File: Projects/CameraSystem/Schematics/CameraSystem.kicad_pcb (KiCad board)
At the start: 2 copper layers, 100 x 100 mm, 119 parts, among them J1 10118192-0001LF, J10 Conn_02x02_Odd_Even, J11 Conn_01x06, J12 Conn_01x06, J13 Conn_02x02_Odd_Even, J14 Conn_02x05_Odd_Even, J2 Conn_02x03_Odd_Even, J3 Conn_01x02, J4 Conn_01x03, J5 Conn_01x02, J6 Conn_02x02_Odd_Even, J7 Conn_02x02_Odd_Even, J8 DM3D-SF, J9 Conn_02x02_Odd_Even, K1 TouchPad, K2 TouchPad, K3 TouchPad, K4 TouchPad, K5 TouchPad, K6 TouchPad, K7 TouchPad, Q1 BC846B_215, Q2 BC846B_215, Q3 BC846B_215, Q4 BC846B_215, U1 CH340, U10 AT42QT1070-SSUR, U2 AZ1117CD-3.3TRG1DICT-ND, U3 ATMEGA16A-AU, U4 ESP8266, U5 MC74HC125ADTR2G, U6 OV7670, U7 SIT2001BI-S2-33E-24.000000G, U8 PCA9306D_118, U9 LCD_2x16_w_i2c, Y1 ABLS-12.000MHZ-B2-T, Y2 ABLS2-10.000MHZ-D4Y-T

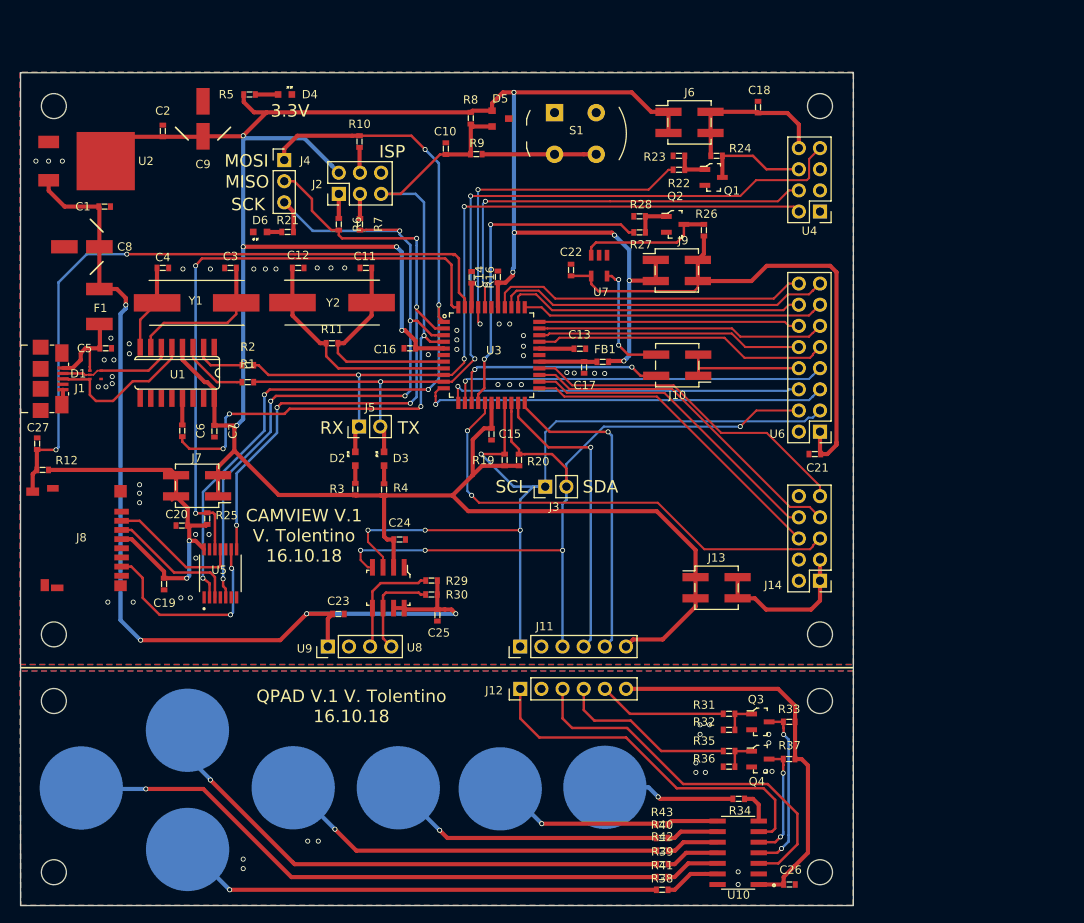
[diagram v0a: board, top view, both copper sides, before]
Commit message: camera was updated
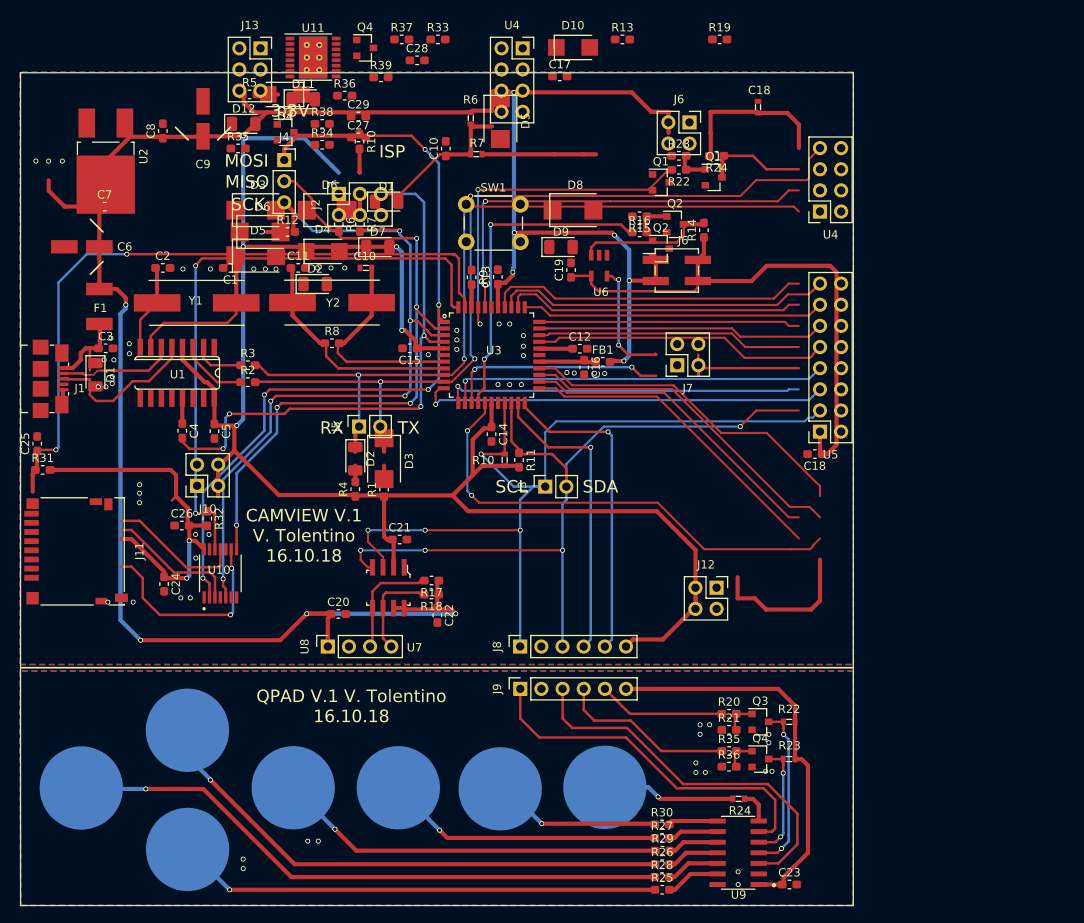
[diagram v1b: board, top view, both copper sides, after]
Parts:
- removed the C6 at (39.4, 63.0)
- removed the D1 at (29.0, 56.3)
- removed the D2 at (60.2, 66.3)
- removed the D3 at (63.7, 66.3)
- removed the D4 at (51.8, 22.6)
- removed the D5 at (77.6, 25.5)
- removed the D6 at (48.8, 39.1)
- removed J14: Conn_02x05_Odd_Even, Pin_Headers:Pin_Header_Straight_2x05_Pitch2.54mm
- removed the Q1 at (103.2, 32.6)
- removed the Q2 at (98.6, 38.2)
- removed the Q3 at (108.8, 97.9)
- removed the Q4 at (108.8, 102.4)
- removed the R35 at (105.1, 101.4)
- removed the R36 at (105.1, 103.3)
- removed R40, R41, R42, R43: 4K7, digikey-footprints:0603
- removed REF** (x8): MountingHole_3mm, Mounting_Holes:MountingHole_3mm
- removed S1: KS-01Q-01, digikey-footprints:PushButton_Round_D12mm_THT_KS-01Q-01
- removed the U4 at (116.0, 36.7)
- removed the U6 at (116.0, 63.1)
- removed the U9 at (56.9, 88.9)
- added C11: 27p, Capacitor_SMD:C_0603_1608Metric_Pad1.05x0.95mm_HandSolder, F.Cu at (53.3, 43.4)
- added C18: 100n, Capacitor_SMD:C_0603_1608Metric_Pad1.05x0.95mm_HandSolder, F.Cu at (115.4, 65.8)
- added C28: 2u2, Capacitor_SMD:C_0603_1608Metric_Pad1.05x0.95mm_HandSolder, F.Cu at (67.6, 18.5)
- added C29: 10u, Capacitor_SMD:C_0603_1608Metric_Pad1.05x0.95mm_HandSolder, F.Cu at (60.6, 25.3)
- added C8: 1u, Capacitor_SMD:C_0603_1608Metric_Pad1.05x0.95mm_HandSolder, F.Cu at (37.1, 27.0)
- added D1: BLUE_LED, LED_SMD:LED_1206_3216Metric, F.Cu at (64.0, 35.5)
- added D1: BLUE_LED, LED_SMD:LED_1206_3216Metric, F.Cu at (29.0, 56.3)
- added D10: SS14, custom-footprints:SMA_DO-214AC, F.Cu at (86.3, 17.0)
- added D11: GREEN_LED, LED_SMD:LED_1206_3216Metric, F.Cu at (53.9, 23.2)
- added D12: RED_LED, LED_SMD:LED_1206_3216Metric, F.Cu at (46.8, 26.1)
- added D2: YELLOW_LED, LED_SMD:LED_1206_3216Metric, F.Cu at (55.4, 45.4)
- added D2: YELLOW_LED, LED_SMD:LED_1206_3216Metric, F.Cu at (60.2, 66.3)
- added D3: SMBJ5.0CA, custom-footprints:SMB_DO-214AA, F.Cu at (48.2, 36.5)
- added D3: SMBJ5.0CA, custom-footprints:SMB_DO-214AA, F.Cu at (63.7, 66.3)
- added D4: SS14, custom-footprints:SMA_DO-214AC, F.Cu at (56.3, 41.5)
- added D4: SS14, custom-footprints:SMA_DO-214AC, F.Cu at (51.8, 22.6)
- added D5: SMBJ5.0CA, custom-footprints:SMB_DO-214AA, F.Cu at (48.2, 42.0)
- added D5: SMBJ5.0CA, custom-footprints:SMB_DO-214AA, F.Cu at (77.6, 25.5)
- added D6: SMBJ5.0CA, custom-footprints:SMB_DO-214AA, F.Cu at (56.8, 36.5)
- added D6: SMBJ5.0CA, custom-footprints:SMB_DO-214AA, F.Cu at (48.8, 39.1)
- added D7: GREEN_LED, LED_SMD:LED_1206_3216Metric, F.Cu at (62.9, 40.9)
- added D8: SMBJ5.0CA, custom-footprints:SMB_DO-214AA, F.Cu at (86.3, 36.5)
- added D9: LED, LED_SMD:LED_1206_3216Metric, F.Cu at (84.9, 40.9)
- added J9: Conn_01x06, Connector_PinSocket_2.54mm:PinSocket_1x06_P2.54mm_Vertical, F.Cu at (80.0, 94.0)
- added Q1: BC847, Package_TO_SOT_SMD:SOT-23, F.Cu at (96.9, 33.2)
- added Q1: BC847, Package_TO_SOT_SMD:SOT-23, F.Cu at (103.2, 32.6)
- added Q2: BC847, Package_TO_SOT_SMD:SOT-23, F.Cu at (96.9, 41.1)
- added Q2: BC847, Package_TO_SOT_SMD:SOT-23, F.Cu at (98.6, 38.2)
- added Q3: BC847, Package_TO_SOT_SMD:SOT-23, F.Cu at (51.8, 27.2)
- added Q3: BC847, Package_TO_SOT_SMD:SOT-23, F.Cu at (108.8, 97.9)
- added Q4: BC847, Package_TO_SOT_SMD:SOT-23, F.Cu at (61.4, 17.0)
- added Q4: BC847, Package_TO_SOT_SMD:SOT-23, F.Cu at (108.8, 102.4)
- added R13: 10k, Resistor_SMD:R_0603_1608Metric_Pad1.05x0.95mm_HandSolder, F.Cu at (92.3, 16.0)
- added R14: 10k, Resistor_SMD:R_0603_1608Metric_Pad1.05x0.95mm_HandSolder, F.Cu at (102.1, 38.9)
- added R15: 10k, Resistor_SMD:R_0603_1608Metric_Pad1.05x0.95mm_HandSolder, F.Cu at (94.3, 37.2)
- added R17: 1K74, Resistor_SMD:R_0603_1608Metric_Pad1.05x0.95mm_HandSolder, F.Cu at (69.4, 81.0)
- added R18: 1K74, Resistor_SMD:R_0603_1608Metric_Pad1.05x0.95mm_HandSolder, F.Cu at (69.3, 82.7)
- added R19: 200k, Resistor_SMD:R_0603_1608Metric_Pad1.05x0.95mm_HandSolder, F.Cu at (104.0, 16.0)
- added R33: 1, Resistor_SMD:R_0603_1608Metric_Pad1.05x0.95mm_HandSolder, F.Cu at (70.1, 16.0)
- added R34: 10k, Resistor_SMD:R_0603_1608Metric_Pad1.05x0.95mm_HandSolder, F.Cu at (56.2, 28.6)
- added R35: 10k, Resistor_SMD:R_0603_1608Metric_Pad1.05x0.95mm_HandSolder, F.Cu at (46.1, 29.1)
- added R35: 10k, Resistor_SMD:R_0603_1608Metric_Pad1.05x0.95mm_HandSolder, F.Cu at (105.1, 101.4)
- added R36: 47k, Resistor_SMD:R_0603_1608Metric_Pad1.05x0.95mm_HandSolder, F.Cu at (58.9, 22.7)
- added R36: 47k, Resistor_SMD:R_0603_1608Metric_Pad1.05x0.95mm_HandSolder, F.Cu at (105.1, 103.3)
- added R37: 560, Resistor_SMD:R_0603_1608Metric_Pad1.05x0.95mm_HandSolder, F.Cu at (65.8, 16.0)
- added R8: 1M, Resistor_SMD:R_0603_1608Metric_Pad1.05x0.95mm_HandSolder, F.Cu at (57.4, 52.5)
- added R9: 10k, Resistor_SMD:R_0603_1608Metric_Pad1.05x0.95mm_HandSolder, F.Cu at (74.2, 44.6)
- added SW1: SW_Push, Button_Switch_THT:SW_PUSH_6mm_H4.3mm, F.Cu at (73.5, 35.8)
- added U11: DRV8833PWP, Package_SO:HTSSOP-16-1EP_4.4x5mm_P0.65mm_EP3.4x5mm_Mask2.46x2.31mm_ThermalVias, F.Cu at (55.1, 18.2)
- added U4: ESP8266, Connector_PinSocket_2.54mm:PinSocket_2x04_P2.54mm_Vertical, F.Cu at (80.3, 17.1)
- added U4: ESP8266, Connector_PinSocket_2.54mm:PinSocket_2x04_P2.54mm_Vertical, F.Cu at (116.0, 36.7)
- added U5: OV7670, Connector_PinSocket_2.54mm:PinSocket_2x08_P2.54mm_Vertical, F.Cu at (116.0, 63.1)
- added U8: LCD_2x16_w_i2c, Connector_PinSocket_2.54mm:PinSocket_1x04_P2.54mm_Vertical, F.Cu at (56.9, 88.9)
- C1, C2: value 1u -> 27p; footprint digikey-footprints:0603 -> Capacitor_SMD:C_0603_1608Metric_Pad1.05x0.95mm_HandSolder
- C10: value 100n -> 27p; footprint digikey-footprints:0603 -> Capacitor_SMD:C_0603_1608Metric_Pad1.05x0.95mm_HandSolder
- C12, C3: value 27p -> 100n; footprint digikey-footprints:0603 -> Capacitor_SMD:C_0603_1608Metric_Pad1.05x0.95mm_HandSolder
- C13, C14, C15, C16, C17, C19, C20, C21, C22, C23, C24, C25, C26, C5: footprint digikey-footprints:0603 -> Capacitor_SMD:C_0603_1608Metric_Pad1.05x0.95mm_HandSolder
- C27: value 100n -> 10n; footprint digikey-footprints:0603 -> Capacitor_SMD:C_0603_1608Metric_Pad1.05x0.95mm_HandSolder
- C4: value 22p -> 100n; footprint digikey-footprints:0603 -> Capacitor_SMD:C_0603_1608Metric_Pad1.05x0.95mm_HandSolder
- C7: value 100n -> 1u; footprint digikey-footprints:0603 -> Capacitor_SMD:C_0603_1608Metric_Pad1.05x0.95mm_HandSolder
- FB1, R2, R4, R5, R7: footprint digikey-footprints:0603 -> Resistor_SMD:R_0603_1608Metric_Pad1.05x0.95mm_HandSolder
- J10, J6, J7: footprint Pin_Headers:Pin_Header_Straight_2x02_Pitch2.54mm_SMD -> Connector_PinSocket_2.54mm:PinSocket_2x02_P2.54mm_Vertical
- J11: value Conn_01x06 -> DM3D-SF; footprint Pin_Headers:Pin_Header_Straight_1x06_Pitch2.54mm -> Connector_Card:microSD_HC_Hirose_DM3D-SF
- J12: value Conn_01x06 -> Conn_02x02_Odd_Even; footprint Pin_Headers:Pin_Header_Straight_1x06_Pitch2.54mm -> Connector_PinSocket_2.54mm:PinSocket_2x02_P2.54mm_Vertical
- J13: value Conn_02x02_Odd_Even -> Conn_02x03_Odd_Even; footprint Pin_Headers:Pin_Header_Straight_2x02_Pitch2.54mm_SMD -> Connector_PinSocket_2.54mm:PinSocket_2x03_P2.54mm_Vertical
- J2: footprint Pin_Headers:Pin_Header_Straight_2x03_Pitch2.54mm -> Connector_PinSocket_2.54mm:PinSocket_2x03_P2.54mm_Vertical
- J3, J5: footprint Pin_Headers:Pin_Header_Straight_1x02_Pitch2.54mm -> Connector_PinSocket_2.54mm:PinSocket_1x02_P2.54mm_Vertical
- J4: footprint Pin_Headers:Pin_Header_Straight_1x03_Pitch2.54mm -> Connector_PinSocket_2.54mm:PinSocket_1x03_P2.54mm_Vertical
- J8: value DM3D-SF -> Conn_01x06; footprint custom-footprints:DM3D-SF -> Connector_PinSocket_2.54mm:PinSocket_1x06_P2.54mm_Vertical
- R1: value 1k -> 560; footprint digikey-footprints:0603 -> Resistor_SMD:R_0603_1608Metric_Pad1.05x0.95mm_HandSolder
- R10: value 330 -> 2K2; footprint digikey-footprints:0603 -> Resistor_SMD:R_0603_1608Metric_Pad1.05x0.95mm_HandSolder
- R11: value 1M -> 2K2; footprint digikey-footprints:0603 -> Resistor_SMD:R_0603_1608Metric_Pad1.05x0.95mm_HandSolder
- R12: value 10k -> 560; footprint digikey-footprints:0603 -> Resistor_SMD:R_0603_1608Metric_Pad1.05x0.95mm_HandSolder
- R16: value 10k -> 4k7; footprint digikey-footprints:0603 -> Resistor_SMD:R_0603_1608Metric_Pad1.05x0.95mm_HandSolder
- R20: value 2K2 -> 4K7; footprint digikey-footprints:0603 -> Resistor_SMD:R_0603_1608Metric_Pad1.05x0.95mm_HandSolder
- R21: value 560 -> 10K; footprint digikey-footprints:0603 -> Resistor_SMD:R_0603_1608Metric_Pad1.05x0.95mm_HandSolder
- R22: value 4K7 -> 10K; footprint digikey-footprints:0603 -> Resistor_SMD:R_0603_1608Metric_Pad1.05x0.95mm_HandSolder
- R23: value 10k -> 10K; footprint digikey-footprints:0603 -> Resistor_SMD:R_0603_1608Metric_Pad1.05x0.95mm_HandSolder
- R24, R25, R26, R27: value 10k -> 4K7; footprint digikey-footprints:0603 -> Resistor_SMD:R_0603_1608Metric_Pad1.05x0.95mm_HandSolder
- R28: value 4k7 -> 4K7; footprint digikey-footprints:0603 -> Resistor_SMD:R_0603_1608Metric_Pad1.05x0.95mm_HandSolder
- R29, R30: value 1K74 -> 4K7; footprint digikey-footprints:0603 -> Resistor_SMD:R_0603_1608Metric_Pad1.05x0.95mm_HandSolder
- R3: value 560 -> 1k; footprint digikey-footprints:0603 -> Resistor_SMD:R_0603_1608Metric_Pad1.05x0.95mm_HandSolder
- R31: value 4K7 -> 10k; footprint digikey-footprints:0603 -> Resistor_SMD:R_0603_1608Metric_Pad1.05x0.95mm_HandSolder
- R32: value 10K -> 10k; footprint digikey-footprints:0603 -> Resistor_SMD:R_0603_1608Metric_Pad1.05x0.95mm_HandSolder
- R38: value 4K7 -> 47k; footprint digikey-footprints:0603 -> Resistor_SMD:R_0603_1608Metric_Pad1.05x0.95mm_HandSolder
- R39: value 4K7 -> 560; footprint digikey-footprints:0603 -> Resistor_SMD:R_0603_1608Metric_Pad1.05x0.95mm_HandSolder
- R6: value 330 -> 10k; footprint digikey-footprints:0603 -> Resistor_SMD:R_0603_1608Metric_Pad1.05x0.95mm_HandSolder
- U2: footprint custom-footprints:TO252-2 -> Package_TO_SOT_SMD:TO-252-2_TabPin1
- moved R38 100.6 mm to (56.2, 26.1)
- moved R39 100.3 mm to (63.3, 20.5)
- moved R31 87.5 mm to (22.7, 67.7)
- moved J13 84.8 mm to (48.8, 17.1)
- moved C26 84.7 mm to (39.4, 74.4)
- moved R21 79.9 mm to (105.1, 98.9)
- moved R28 77.5 mm to (97.0, 116.6)
- moved R26 76.3 mm to (97.1, 115.0), turned to 0 degrees
- moved R27 74.7 mm to (97.0, 111.9), turned to 0 degrees
- moved R25 70.5 mm to (97.1, 118.1), turned to 0 degrees
- moved R32 67.6 mm to (42.4, 73.5), turned to 270 degrees
- moved C23 63.2 mm to (112.3, 117.5)
- moved C19 61.7 mm to (86.1, 43.7), turned to 90 degrees
- moved J10 59.4 mm to (41.2, 69.6)
- moved J7 59.4 mm to (98.9, 55.1)
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- renumbered C11 to C10, C8 to C6, J9 to J6, R19 to R10, R33 to R22, R37 to R23, R34 to R24, R8 to R6, R9 to R7, U5 to U10, U7 to U6, U8 to U7, U10 to U9
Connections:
- C1 pad 1: /Display/VDD_5V0 -> Net-(C1-Pad1)
- C10 pad 1: Net-(C11-Pad1) -> Net-(C10-Pad1)
- C10 pad 1: /Input_Interface/SPI_RST -> Net-(C10-Pad1)
- C13 pad 1: Net-(C13-Pad1) -> /Camera/VDD_3V3
- C16 pad 1: /Camera/VDD_3V3 -> Net-(C16-Pad1)
- C17 pad 1: Net-(C17-Pad1) -> /Camera/VDD_3V3
- C18 pad 1: /Wifi/VDD_3V3_IN -> /Camera/VDD_3V3_IN
- C19 pad 1: /Memory/VDD_3V3_IN -> /Camera/VDD_3V3_IN
- C2 pad 1: /Camera/VDD_3V3 -> Net-(C2-Pad1)
- C20 pad 1: GND -> /Display/VDD_5V0
- C20 pad 2: /Memory/VDD_3V3_IN -> GND
- C21 pad 1: /Camera/VDD_3V3_IN -> /Camera/VDD_3V3
- C22 pad 1: /Camera/VDD_3V3_IN -> Net-(C22-Pad1)
- C23 pad 1: /Display/VDD_5V0 -> /Keypad/VDD_3V3
- C23 pad 2: GND -> /Keypad/QP_GND
- C24 pad 1: /Camera/VDD_3V3 -> /Memory/VDD_3V3_IN
- C25 pad 1: /Display/VDD_5V0 -> /Memory/_SD_DET
- C26 pad 1: /Keypad/VDD_3V3 -> GND
- C26 pad 2: /Keypad/QP_GND -> /Memory/VDD_3V3_IN
- C27 pad 1: /Memory/_SD_DET -> Net-(C27-Pad1)
- C27 pad 2: GND -> /Motor/VDD_3V3_CON_IN
- C4 pad 2: GND -> /Microcontroller/U2_SPI_RST
- C5 pad 1: Net-(C5-Pad1) -> /Camera/VDD_3V3
- C7 pad 1: /Camera/VDD_3V3 -> /Display/VDD_5V0
- F1 pad 2: Net-(C5-Pad1) -> Net-(C3-Pad1)
- FB1 pad 1: Net-(C17-Pad1) -> Net-(C16-Pad1)
- J1 pad 1: Net-(C5-Pad1) -> Net-(C3-Pad1)
- J1 pad 4: (no net) -> Net-(J1-Pad4)
- J10 pad 1: Net-(J10-Pad1) -> /Camera/VDD_3V3
- J10 pad 2: /Camera/CAM_CLK -> /Memory/VDD_3V3_IN
- J10 pad 3: Net-(J10-Pad1) -> /Camera/VDD_3V3
- J10 pad 4: Net-(J10-Pad4) -> /Memory/VDD_3V3_IN
- J11 pad 1: /Camera/SCL_3V3 -> Net-(J11-Pad1)
- J11 pad 2: GND -> /Memory/SD_CS_IN
- J11 pad 3: /Camera/SDA_3V3 -> /Memory/SD_DATA_IN
- J11 pad 4: /Microcontroller/QT_CHN -> /Memory/VDD_3V3_IN
- J11 pad 5: /Microcontroller/QT_RST -> /Memory/SD_CLK_IN
- J11 pad 6: /Camera/VDD_3V3 -> GND
- J12 pad 1: /Keypad/SCL_3V3 -> /Camera/VDD_3V3
- J12 pad 2: /Keypad/QP_GND -> /Motor/VDD_3V3_CON_IN
- J12 pad 3: /Keypad/SDA_3V3 -> /Camera/VDD_3V3
- J12 pad 4: /Keypad/QT_CHN -> /Motor/VDD_3V3_CON_IN
- J13 pad 1: /Camera/VDD_3V3 -> /Motor/M_PWM_OUT_1
- J13 pad 2: /Motor/VDD_3V3_CON_IN -> /Motor/M_PWM_OUT_1
- J13 pad 3: /Camera/VDD_3V3 -> /Motor/M_PWM_OUT_2
- J13 pad 4: /Motor/VDD_3V3_CON_IN -> /Motor/M_PWM_OUT_2
- J2 pad 1: Net-(J2-Pad1) -> /Microcontroller/MISO
- J2 pad 3: Net-(J2-Pad3) -> /Microcontroller/SCK
- J2 pad 4: Net-(J2-Pad4) -> /Microcontroller/MOSI
- J2 pad 5: /Input_Interface/SPI_RST -> /Microcontroller/U2_SPI_RST
- J6 pad 2: /Wifi/VDD_3V3_IN -> /Camera/VDD_3V3_IN
- J6 pad 4: /Wifi/VDD_3V3_IN -> /Camera/VDD_3V3_IN
- J7 pad 1: /Camera/VDD_3V3 -> Net-(J7-Pad1)
- J7 pad 2: /Memory/VDD_3V3_IN -> /Camera/CAM_CLK
- J7 pad 3: /Camera/VDD_3V3 -> Net-(J7-Pad1)
- J7 pad 4: /Memory/VDD_3V3_IN -> Net-(J7-Pad4)
- J8 pad 1: (no net) -> /Camera/SCL_3V3
- J8 pad 2: /Memory/SD_CS_IN -> GND
- J8 pad 3: /Memory/SD_DATA_IN -> /Camera/SDA_3V3
- J8 pad 4: /Memory/VDD_3V3_IN -> /Microcontroller/QT_CHN
- J8 pad 5: (no net) -> /Microcontroller/QT_RST
- J8 pad 6: GND -> /Camera/VDD_3V3
- R1 pad 1: Net-(R1-Pad1) -> /Camera/VDD_3V3
- R1 pad 2: /Microcontroller/SPI_TX -> Net-(D1-Pad2)
- R10 pad 1: /Microcontroller/MOSI -> /Camera/SCL_3V3
- R10 pad 2: Net-(J2-Pad4) -> /Camera/VDD_3V3
- R11 pad 1: Net-(C12-Pad1) -> /Camera/SDA_3V3
- R11 pad 2: Net-(C11-Pad1) -> /Camera/VDD_3V3
- R12 pad 1: /Memory/_SD_DET -> Net-(D9-Pad2)
- R12 pad 2: /Memory/VDD_3V3_IN -> /Microcontroller/SCK
- R16 pad 1: GND -> /Camera/CAM_XCLK_CTL
- R16 pad 2: Net-(R16-Pad2) -> Net-(Q1-Pad1)
- R2 pad 2: /Microcontroller/SPI_RX -> /Microcontroller/UC_SPI_TX
- R20 pad 1: /Camera/SDA_3V3 -> /Keypad/QT_RST
- R20 pad 2: /Camera/VDD_3V3 -> Net-(Q2-Pad1)
- R21 pad 1: Net-(D6-Pad2) -> /Keypad/QP_GND
- R21 pad 2: /Microcontroller/SCK -> Net-(Q2-Pad1)
- R22 pad 1: Net-(Q1-Pad1) -> /Keypad/_QT_RST_IN
- R22 pad 2: /Microcontroller/WIFI_RST -> /Keypad/VDD_3V3
- R23 pad 1: /Keypad/_QT_CHN_IN -> /Keypad/QT_CHN
- R23 pad 1: GND -> /Keypad/QT_CHN
- R23 pad 2: Net-(Q1-Pad1) -> /Keypad/VDD_3V3
- R24 pad 1: Net-(R34-Pad1) -> Net-(R24-Pad1)
- R24 pad 1: Net-(Q1-Pad3) -> Net-(R24-Pad1)
- R24 pad 2: /Wifi/VDD_3V3_IN -> Net-(K1-Pad1)
- R25 pad 1: /Microcontroller/CS -> Net-(K2-Pad1)
- R25 pad 2: /Memory/VDD_3V3_IN -> Net-(R25-Pad2)
- R26 pad 1: /Camera/VDD_3V3_IN -> Net-(K4-Pad1)
- R26 pad 2: Net-(Q2-Pad3) -> Net-(R26-Pad2)
- R27 pad 1: Net-(Q2-Pad1) -> Net-(K6-Pad1)
- R27 pad 2: GND -> Net-(R27-Pad2)
- R28 pad 1: /Camera/CAM_XCLK_CTL -> Net-(K3-Pad1)
- R28 pad 2: Net-(Q2-Pad1) -> Net-(R28-Pad2)
- R29 pad 1: /Display/VDD_5V0 -> Net-(K5-Pad1)
- R29 pad 2: /Display/SDA_5V0 -> Net-(R29-Pad2)
- R3 pad 1: /Camera/VDD_3V3 -> Net-(D2-Pad1)
- R3 pad 2: Net-(D2-Pad2) (its old number) -> /Microcontroller/UC_SPI_RX
- R30 pad 1: /Display/VDD_5V0 -> Net-(K7-Pad1)
- R30 pad 2: /Display/SCL_5V0 -> Net-(R30-Pad2)
- R31 pad 1: /Keypad/QT_RST -> /Memory/_SD_DET
- R31 pad 2: Net-(Q3-Pad1) -> /Memory/VDD_3V3_IN
- R32 pad 1: /Keypad/QP_GND -> /Microcontroller/CS
- R32 pad 2: Net-(Q3-Pad1) -> /Memory/VDD_3V3_IN
- R38 pad 1: Net-(K2-Pad1) -> Net-(Q4-Pad1)
- R38 pad 2: Net-(R38-Pad2) -> Net-(D11-Pad1)
- R39 pad 1: Net-(K4-Pad1) -> /Motor/VDD_3V3_CON_IN
- R39 pad 2: Net-(R39-Pad2) -> Net-(D12-Pad2)
- R6 pad 2: /Input_Interface/SPI_RST -> /Microcontroller/U2_SPI_RST
- R6 pad 1: Net-(J2-Pad1) -> /Camera/VDD_3V3
- R6 pad 2: /Microcontroller/MISO -> /Microcontroller/U2_SPI_RST
- R7 pad 1: /Input_Interface/SPI_RST -> /Microcontroller/U2_SPI_RST
- R7 pad 2: Net-(R9-Pad2) -> Net-(R7-Pad2)
- R7 pad 1: Net-(J2-Pad3) -> /Microcontroller/U2_SPI_RST
- R7 pad 2: /Microcontroller/SCK -> Net-(R7-Pad2)
- U1 pad 10: (no net) -> Net-(U1-Pad10)
- U1 pad 11: (no net) -> Net-(U1-Pad11)
- U1 pad 12: (no net) -> Net-(U1-Pad12)
- U1 pad 13: Net-(C6-Pad1) -> Net-(C4-Pad1)
- U1 pad 14: (no net) -> Net-(U1-Pad14)
- U1 pad 15: (no net) -> Net-(U1-Pad15)
- U1 pad 2: Net-(R2-Pad1) -> Net-(D4-Pad1)
- U1 pad 3: Net-(R1-Pad1) -> Net-(R2-Pad1)
- U1 pad 7: Net-(C3-Pad1) -> Net-(C1-Pad1)
- U1 pad 8: Net-(C4-Pad1) -> Net-(C2-Pad1)
- U1 pad 9: (no net) -> Net-(U1-Pad9)
- U10 pad 2: /Microcontroller/MOSI -> /Memory/SD_DATA_OUT
- U10 pad 3: /Memory/SD_DATA_IN -> /Microcontroller/MISO
- U10 pad 6: (no net) -> /Memory/SD_SCK_IN
- U10 pad 8: /Microcontroller/MISO -> /Memory/SD_DATA_IN
- U10 pad 9: /Memory/SD_DATA_OUT -> /Microcontroller/MOSI
- U3 pad 10: /Microcontroller/SPI_TX -> /Microcontroller/UC_SPI_TX
- U3 pad 16: /Microcontroller/M_PWM -> /Microcontroller/M_NSLEEP
- U3 pad 23: /Microcontroller/M_DIR -> /Microcontroller/M_PWM_IN_1
- U3 pad 24: /Microcontroller/M_EN -> /Microcontroller/M_PWM_IN_2
- U3 pad 27: Net-(C17-Pad1) -> Net-(C16-Pad1)
- U3 pad 29: Net-(C13-Pad1) -> Net-(C12-Pad1)
- U3 pad 4: /Input_Interface/SPI_RST -> /Microcontroller/U2_SPI_RST
- U3 pad 42: Net-(R16-Pad2) -> Net-(R9-Pad2)
- U3 pad 7: Net-(C11-Pad1) -> Net-(C10-Pad1)
- U3 pad 8: Net-(C12-Pad1) -> Net-(C11-Pad1)
- U3 pad 9: /Microcontroller/SPI_RX -> /Microcontroller/UC_SPI_RX
- U6 pad 2: (no net) -> Net-(U6-Pad2)
- U6 pad 3: Net-(Q2-Pad3) -> Net-(Q1-Pad3)
- U6 pad 5: Net-(J10-Pad4) -> Net-(J7-Pad4)
- U7 pad 7: /Display/VDD_5V0 -> Net-(C22-Pad1)
- U7 pad 8: /Display/VDD_5V0 -> Net-(C22-Pad1)
- U9 pad 10: Net-(R42-Pad2) -> Net-(R29-Pad2)
- U9 pad 11: Net-(R39-Pad2) -> Net-(R26-Pad2)
- U9 pad 12: Net-(R41-Pad2) -> Net-(R28-Pad2)
- U9 pad 13: Net-(R38-Pad2) -> Net-(R25-Pad2)
- U9 pad 5: /Keypad/_QT_CHN_IN -> /Keypad/QT_CHN
- U9 pad 7: Net-(R34-Pad1) -> Net-(R24-Pad1)
- U9 pad 8: Net-(R43-Pad2) -> Net-(R30-Pad2)
- U9 pad 9: Net-(R40-Pad2) -> Net-(R27-Pad2)
- Y1 pad 1: Net-(C3-Pad1) -> Net-(C1-Pad1)
- Y1 pad 2: Net-(C4-Pad1) -> Net-(C2-Pad1)
- Y2 pad 1: Net-(C11-Pad1) -> Net-(C10-Pad1)
- Y2 pad 2: Net-(C12-Pad1) -> Net-(C11-Pad1)
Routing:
- net /Microcontroller/M_PWM: track 57.3 -> 0.00 mm, vias 2 -> 0
- net /Microcontroller/M_NSLEEP: track 0.00 -> 57.3 mm, vias 0 -> 2
- net /Microcontroller/M_PWM_IN_1: track 0.00 -> 38.6 mm
- net /Microcontroller/M_DIR: track 38.6 -> 0.00 mm
- net /Microcontroller/M_PWM_IN_2: track 0.00 -> 37.9 mm
- net /Microcontroller/M_EN: track 37.9 -> 0.00 mm
- net Net-(C10-Pad1): track 0.00 -> 25.5 mm
- net /Microcontroller/MOSI: track 99.6 -> 124.6 mm, vias 5 -> 7
- net /Memory/SD_DATA_OUT: track 25.0 -> 0.00 mm, vias 2 -> 0
- net Net-(C12-Pad1): track 27.4 -> 4.18 mm
- net Net-(C3-Pad1): track 18.2 -> 0.00 mm
- net Net-(C1-Pad1): track 0.00 -> 18.2 mm
- net /Microcontroller/MISO: track 79.8 -> 95.8 mm
- net /Memory/SD_DATA_IN: track 16.0 -> 0.00 mm
- net /Camera/CAM_CLK: track 26.7 -> 42.1 mm
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
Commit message: SP specs updated
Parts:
- added REF**: M2, MountingHole:MountingHole_2.2mm_M2, F.Cu at (23.1, 94.5)
- added REF**: M2, MountingHole:MountingHole_2.2mm_M2, F.Cu at (23.1, 116.9)
- added REF**: M2, MountingHole:MountingHole_2.2mm_M2, F.Cu at (116.9, 116.9)
- added REF**: M2, MountingHole:MountingHole_2.2mm_M2, F.Cu at (116.9, 94.5)
- added REF**: M2, MountingHole:MountingHole_2.2mm_M2, F.Cu at (116.9, 23.1)
- added REF**: M2, MountingHole:MountingHole_2.2mm_M2, F.Cu at (116.9, 88.3)
- added REF**: M2, MountingHole:MountingHole_2.2mm_M2, F.Cu at (23.1, 88.3)
- added REF**: M2, MountingHole:MountingHole_2.2mm_M2, F.Cu at (23.1, 23.1)
- C10, C18: footprint digikey-footprints:0603 -> Capacitor_SMD:C_0603_1608Metric_Pad1.05x0.95mm_HandSolder
- J6: footprint Pin_Headers:Pin_Header_Straight_2x02_Pitch2.54mm_SMD -> Connector_PinSocket_2.54mm:PinSocket_2x02_P2.54mm_Vertical
- R10, R22, R23, R24, R6, R7: footprint digikey-footprints:0603 -> Resistor_SMD:R_0603_1608Metric_Pad1.05x0.95mm_HandSolder
- U2: footprint Package_TO_SOT_SMD:TO-252-2_TabPin1 -> Package_TO_SOT_SMD:TO-252-2
- moved D1 37.2 mm to (64.9, 66.0), turned to 180 degrees
- moved D6 34.6 mm to (24.5, 48.8), turned to 180 degrees
- moved D3 33.0 mm to (31.0, 61.5)
- moved D5 20.2 mm to (31.0, 52.5), turned to 90 degrees
- moved C3 10.3 mm to (25.0, 44.2), turned to 180 degrees
- moved C7 5.69 mm to (24.9, 33.8), turned to 180 degrees
- moved F1 4.02 mm to (30.5, 44.2), turned to 180 degrees
- moved C6 2.84 mm to (25.1, 39.1)
- moved U2 2.68 mm to (30.0, 27.9), turned to 0 degrees
- moved D2 1.43 mm to (58.8, 66.0), turned to 0 degrees
- moved U1 1.27 mm to (40.1, 56.0)
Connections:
- J1 pad 4: Net-(J1-Pad4) -> (no net)
- J11 pad 1: Net-(J11-Pad1) -> (no net)
- J11 pad 5: /Memory/SD_CLK_IN -> (no net)
- J11 pad 8: Net-(J11-Pad8) -> (no net)
- J5 pad 1: /Microcontroller/SPI_RX -> (no net)
- J5 pad 2: /Microcontroller/SPI_TX -> (no net)
- U1 pad 10: Net-(U1-Pad10) -> (no net)
- U1 pad 11: Net-(U1-Pad11) -> (no net)
- U1 pad 12: Net-(U1-Pad12) -> (no net)
- U1 pad 14: Net-(U1-Pad14) -> (no net)
- U1 pad 15: Net-(U1-Pad15) -> (no net)
- U1 pad 9: Net-(U1-Pad9) -> (no net)
- U10 pad 6: /Memory/SD_SCK_IN -> (no net)
- U6 pad 2: Net-(U6-Pad2) -> (no net)
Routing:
- net /Microcontroller/SPI_TX: track 101.8 -> 0.00 mm, vias 3 -> 0
- net /Microcontroller/UC_SPI_TX: track 0.00 -> 98.6 mm, vias 0 -> 3
- net /Display/VDD_5V0: track 121.6 -> 100.0 mm
- net /Input_Interface/USB_DP: track 18.7 -> 0.00 mm
- net /Memory/SD_CS_IN: track 16.2 -> 0.00 mm
- net /Microcontroller/MISO: track 95.8 -> 79.8 mm
- net /Input_Interface/USB_DN: track 14.0 -> 0.00 mm
- net Net-(C5-Pad1): track 11.5 -> 0.00 mm
- net Net-(R2-Pad1): track 14.7 -> 5.38 mm
- net /Memory/VDD_3V3_IN: track 44.3 -> 36.1 mm
- net /Camera/VDD_3V3: track 359.3 -> 351.2 mm
- net /Microcontroller/SPI_RX: track 95.0 -> 91.8 mm
- net Net-(D4-Pad1): track 0.00 -> 2.51 mm
- net Net-(D3-Pad2): track 2.18 -> 0.00 mm
- net Net-(D2-Pad2): track 2.13 -> 0.00 mm
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
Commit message: camera layout updated
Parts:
- removed the C10 at (71.1, 29.1)
- removed the C18 at (108.6, 24.1)
- removed the D1 at (64.0, 35.5)
- removed the D2 at (55.4, 45.4)
- removed the D3 at (48.2, 36.5)
- removed the D3 at (31.0, 61.5)
- removed the D4 at (56.3, 41.5)
- removed the D5 at (77.6, 25.5)
- removed the D6 at (48.8, 39.1)
- removed the J6 at (98.8, 43.7)
- removed the Q1 at (103.2, 32.6)
- removed the Q2 at (96.9, 41.1)
- removed the Q3 at (51.8, 27.2)
- removed the Q4 at (61.4, 17.0)
- removed the R10 at (60.7, 28.3)
- removed the R22 at (99.1, 31.6)
- removed the R23 at (99.1, 30.0)
- removed the R24 at (103.6, 30.0)
- removed the R35 at (46.1, 29.1)
- removed the R36 at (58.9, 22.7)
- removed the R6 at (58.2, 38.2)
- removed the R7 at (60.8, 38.2)
- removed REF** (x8): M2, MountingHole:MountingHole_2.2mm_M2
- removed the U4 at (116.0, 36.7)
- added D3: SMBJ5.0CA, custom-footprints:SMB_DO-214AA, F.Cu at (31.0, 60.9)
- moved D11 108.0 mm to (143.6, 83.3)
- moved D12 106.8 mm to (126.3, 97.4)
- moved R38 106.4 mm to (140.6, 90.9)
- moved R39 102.5 mm to (130.8, 97.7), turned to 180 degrees
- moved C28 97.8 mm to (130.8, 93.1)
- moved R33 97.8 mm to (133.3, 90.6)
- moved R37 97.8 mm to (129.0, 90.6)
- moved R34 95.7 mm to (140.7, 73.6)
- moved C27 93.6 mm to (135.9, 83.4)
- moved U11 90.0 mm to (116.0, 84.5), turned to 90 degrees
- moved J13 89.3 mm to (116.0, 75.9), turned to 180 degrees
- moved C29 87.8 mm to (129.8, 79.2)
- moved U4 41.8 mm to (116.0, 38.8), turned to 180 degrees
- moved D4 40.2 mm to (54.9, 62.6)
- moved D7 21.2 mm to (52.3, 22.6), turned to 180 degrees
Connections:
- net Net-(C3-Pad1) renamed /Input_Interface/USB_VCC
- U4 pad 3: Net-(U4-Pad3) -> (no net)
- U4 pad 5: Net-(U4-Pad5) -> (no net)
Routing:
- net /Camera/VDD_3V3: track 351.2 -> 274.3 mm
- net /Microcontroller/SPI_RX: track 91.8 -> 22.7 mm, vias 3 -> 2
- net /Microcontroller/MOSI: track 124.6 -> 85.0 mm
- net /Microcontroller/SCK: track 91.9 -> 71.2 mm
- net /Wifi/VDD_3V3_IN: track 19.4 -> 0.00 mm
- net /Motor/VDD_3V3_CON_IN: track 18.4 -> 0.00 mm
- net /Input_Interface/SPI_RST: track 85.7 -> 68.7 mm
- net Net-(Q1-Pad3): track 12.4 -> 0.00 mm
- net /Display/VDD_5V0: track 100.0 -> 90.3 mm
- net /Keypad/QT_CHN: track 21.3 -> 13.9 mm
- net /Input_Interface/USB_DP: track 0.00 -> 6.59 mm
- net /Input_Interface/USB_DN: track 0.00 -> 6.38 mm
- net /Microcontroller/UC_SPI_TX: track 98.6 -> 93.2 mm
- net /Microcontroller/MISO: track 79.8 -> 74.9 mm
- net Net-(Q2-Pad3): track 16.4 -> 11.7 mm
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- added copper zone on F.Cu, net /Camera/VDD_3V3
- added copper zone on F.Cu, net /Display/VDD_5V0
- added copper zone on F.Cu, net /Input_Interface/USB_VCC

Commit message: camera layout updated
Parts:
- removed J4: Conn_01x03, Connector_PinSocket_2.54mm:PinSocket_1x03_P2.54mm_Vertical
- added REF**: MountingHole_2.2mm_M2, MountingHole:MountingHole_2.2mm_M2, F.Cu at (23.0, 88.1)
- added REF**: MountingHole_2.2mm_M2, MountingHole:MountingHole_2.2mm_M2, F.Cu at (23.0, 94.7)
- added REF**: MountingHole_2.2mm_M2, MountingHole:MountingHole_2.2mm_M2, F.Cu at (23.0, 117.1)
- added REF**: MountingHole_2.2mm_M2, MountingHole:MountingHole_2.2mm_M2, F.Cu at (117.0, 117.1)
- added REF**: MountingHole_2.2mm_M2, MountingHole:MountingHole_2.2mm_M2, F.Cu at (117.0, 94.7)
- added REF**: MountingHole_2.2mm_M2, MountingHole:MountingHole_2.2mm_M2, F.Cu at (116.9, 88.1)
- added REF**: MountingHole_2.2mm_M2, MountingHole:MountingHole_2.2mm_M2, F.Cu at (117.0, 22.9)
- added REF**: MountingHole_2.2mm_M2, MountingHole:MountingHole_2.2mm_M2, F.Cu at (22.9, 22.8)
- moved R19 77.4 mm to (70.3, 85.6), turned to 90 degrees
- moved Q2 60.6 mm to (108.7, 97.9)
- moved D11 38.9 mm to (104.8, 83.9), turned to 180 degrees
- moved R34 36.1 mm to (104.7, 69.7), turned to 180 degrees
- moved C27 34.2 mm to (101.9, 79.6), turned to 180 degrees
- moved D10 34.0 mm to (112.1, 39.2), turned to 90 degrees
- moved R35 33.7 mm to (104.7, 67.8), turned to 180 degrees
- moved R38 33.7 mm to (107.0, 88.0), turned to 180 degrees
- moved R36 33.6 mm to (110.6, 70.2)
- moved C17 32.9 mm to (116.9, 27.5), turned to 90 degrees
- moved C29 29.2 mm to (101.2, 73.4), turned to 90 degrees
- moved R37 29.1 mm to (101.0, 82.5), turned to 270 degrees
- moved R39 27.6 mm to (108.4, 81.6), turned to 0 degrees
- moved D9 27.5 mm to (60.9, 27.6), turned to 270 degrees
- moved C28 26.2 mm to (108.3, 79.7), turned to 180 degrees
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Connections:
- J13 pad 1: /Motor/M_PWM_OUT_1 -> /Motor/M_PWM_OUT_2
- J13 pad 2: /Motor/M_PWM_OUT_1 -> /Motor/M_PWM_OUT_2
- J13 pad 3: /Motor/M_PWM_OUT_2 -> /Motor/M_PWM_OUT_1
- J13 pad 4: /Motor/M_PWM_OUT_2 -> /Motor/M_PWM_OUT_1
- J5 pad 1: (no net) -> /Microcontroller/UC_SPI_RX
- J5 pad 2: (no net) -> /Microcontroller/UC_SPI_TX
- J7 pad 2: /Camera/CAM_CLK -> Net-(J7-Pad2)
- J7 pad 4: Net-(J7-Pad4) -> /Camera/CAM_CLK
- U6 pad 5: Net-(J7-Pad4) -> Net-(J7-Pad2)
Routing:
- net /Microcontroller/UC_SPI_RX: track 0.00 -> 82.2 mm, vias 0 -> 3
- net /Microcontroller/U2_SPI_RST: track 0.00 -> 79.0 mm, vias 0 -> 5
- net /Camera/VDD_3V3: track 274.3 -> 351.6 mm
- net /Input_Interface/SPI_RST: track 68.7 -> 0.00 mm, vias 4 -> 0
- net /Microcontroller/SENSOR2: track 39.6 -> 84.0 mm, vias 0 -> 2
- net /Motor/VDD_3V3_CON_IN: track 0.00 -> 40.1 mm
- net /Camera/CAM_D2: track 36.2 -> 68.4 mm
- net Net-(Q3-Pad1): track 0.00 -> 29.7 mm, vias 0 -> 2
- net /Memory/SD_DATA_OUT: track 0.00 -> 28.7 mm, vias 0 -> 2
- net /Keypad/QT_CHN: track 13.9 -> 41.2 mm, vias 0 -> 2
- net /Memory/SD_DATA_IN: track 0.00 -> 26.1 mm, vias 0 -> 2
- net /Memory/SD_CS_IN: track 0.00 -> 24.2 mm
- net /Microcontroller/WIFI_RST: track 38.8 -> 62.9 mm
- net /Microcontroller/SPI_RX: track 22.7 -> 0.00 mm, vias 2 -> 0
- net /Camera/CAM_D5: track 34.7 -> 57.0 mm
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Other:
- board text added: "CAMVIEW V.2 V. Tolentino 16.04.19"
- board text added: "GND"
- board text added: "QPAD V.1 V. Tolentino 16.04.19"
- board text added: "RST"
- board text added: "VCC"
- board text removed: "CAMVIEW V.1 V. Tolentino 16.10.18"
- board text removed: "QPAD V.1 V. Tolentino 16.10.18"

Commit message: camera layout updated
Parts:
- moved REF** 0.31 mm to (117.0, 95.0)
- moved C12 0.28 mm to (87.0, 52.9)
- moved REF** 0.26 mm to (23.0, 95.0)
- moved REF** 0.21 mm to (23.0, 23.0)
- moved REF** 0.14 mm to (23.0, 88.0)
- moved REF** 0.14 mm to (117.0, 23.0)
- moved REF** 0.10 mm to (117.0, 88.0)
- moved REF** 0.09 mm to (23.0, 117.0)
- moved REF** 0.09 mm to (117.0, 117.0)
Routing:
- net /Camera/VDD_3V3: track 351.6 -> 46.7 mm, vias 11 -> 21
- net Net-(Q1-Pad3): track 2.83 -> 6.62 mm
- net /Display/VDD_5V0: track 92.6 -> 95.4 mm
- net /Memory/VDD_3V3_IN: track 45.3 -> 46.2 mm
- net GND: vias 69 -> 76
- added copper zone on B.Cu, net /Camera/VDD_3V3
